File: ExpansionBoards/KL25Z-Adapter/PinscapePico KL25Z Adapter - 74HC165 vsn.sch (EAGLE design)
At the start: 26 parts, among them IC1 SN74HC165DR, IC2 SN74HC165DR, IC3 SN74HC165DR, IC4 LIS3DHTR, IC5 ADS1115IDGSR, IC6 PCA9555APW,118, SW1 TS-1187A-B-A-B

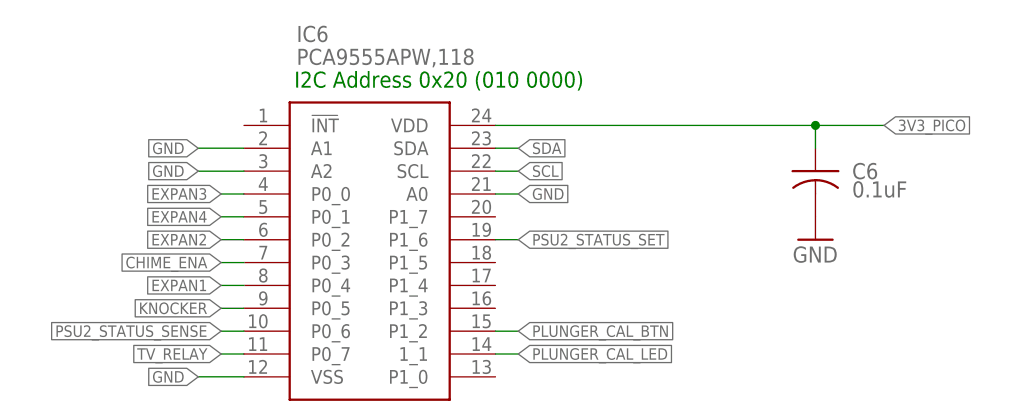
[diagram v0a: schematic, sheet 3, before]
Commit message: Finish JSON configuration for 74HC165, tweaks to 74HC165 layout
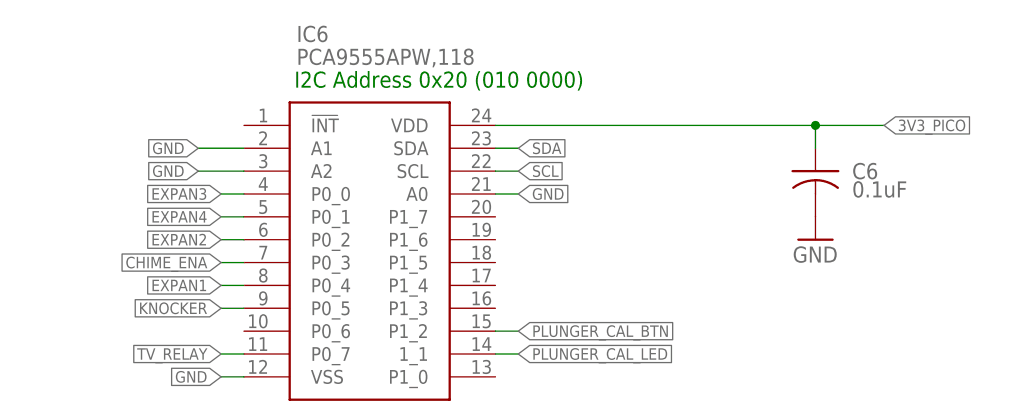
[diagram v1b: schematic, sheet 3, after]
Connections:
- net PSU2_STATUS_SENSE: now also RASPBERRY_PI_PICO.GP20; no longer IC6.P0_6
- net PSU2_STATUS_SET: now also RASPBERRY_PI_PICO.GP21; no longer IC6.P1_6
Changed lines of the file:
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@@
 <label x="246.38" y="101.6" size="1.27" layer="95" xref="yes"/>
+</segment>
+<segment>
+<pinref part="RASPBERRY_PI_PICO" gate="G$1" pin="GP21"/>
+<wire x1="73.66" y1="33.02" x2="71.12" y2="33.02" width="0.1524" layer="91"/>
+<label x="73.66" y="33.02" size="1.27" layer="95" xref="yes"/>
 </segment>
 </net>
@@
 <wire x1="243.84" y1="76.2" x2="246.38" y2="76.2" width="0.1524" layer="91"/>
 <label x="246.38" y="76.2" size="1.27" layer="95" xref="yes"/>
+</segment>
+<segment>
+<pinref part="RASPBERRY_PI_PICO" gate="G$1" pin="GP20"/>
+<wire x1="73.66" y1="30.48" x2="71.12" y2="30.48" width="0.1524" layer="91"/>
+<label x="73.66" y="30.48" size="1.27" layer="95" xref="yes"/>
 </segment>
 </net>
@@
 </segment>
 </net>
-<net name="PSU2_STATUS_SENSE" class="0">
-<segment>
-<pinref part="IC6" gate="G$1" pin="P0_6"/>
-<wire x1="30.48" y1="10.16" x2="27.94" y2="10.16" width="0.1524" layer="91"/>
-<label x="27.94" y="10.16" size="1.27" layer="95" rot="R180" xref="yes"/>
-</segment>
-</net>
-<net name="PSU2_STATUS_SET" class="0">
-<segment>
-<wire x1="58.42" y1="20.32" x2="60.96" y2="20.32" width="0.1524" layer="91"/>
-<label x="60.96" y="20.32" size="1.27" layer="95" xref="yes"/>
-<pinref part="IC6" gate="G$1" pin="P1_6"/>
-</segment>
-</net>
 <net name="CHIME_ENA" class="0">
 <segment>
@@
 <segment>
 <pinref part="IC6" gate="G$1" pin="VSS"/>
-<wire x1="25.4" y1="5.08" x2="30.48" y2="5.08" width="0.1524" layer="91"/>
-<label x="25.4" y="5.08" size="1.27" layer="95" rot="R180" xref="yes"/>
-</segment>
-<segment>
+<wire x1="27.94" y1="5.08" x2="30.48" y2="5.08" width="0.1524" layer="91"/>
+<label x="27.94" y="5.08" size="1.27" layer="95" rot="R180" xref="yes"/>
+</segment>
+<segment>

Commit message: minor board updates
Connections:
- net BUTTON12: now also IC2.F, RN2.4; no longer IC2.C, RN2.8
- net BUTTON13: now also IC2.C, RN2.8; no longer IC2.F, RN2.4
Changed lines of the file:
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@@
 <net name="BUTTON13" class="0">
+<segment>
+<wire x1="22.86" y1="43.18" x2="25.4" y2="43.18" width="0.1524" layer="91"/>
+<label x="22.86" y="43.18" size="1.27" layer="95" rot="R180" xref="yes"/>
+<pinref part="RN2" gate="G$1" pin="8"/>
+</segment>
+<segment>
+<wire x1="134.62" y1="50.8" x2="137.16" y2="50.8" width="0.1524" layer="91"/>
+<label x="137.16" y="50.8" size="1.27" layer="95" rot="MR180" xref="yes"/>
+<pinref part="IC2" gate="G$1" pin="C"/>
+</segment>
+</net>
+<net name="BUTTON12" class="0">
 <segment>
 <wire x1="53.34" y1="43.18" x2="50.8" y2="43.18" width="0.1524" layer="91"/>
@@
 </segment>
 </net>
-<net name="BUTTON12" class="0">
-<segment>
-<wire x1="22.86" y1="43.18" x2="25.4" y2="43.18" width="0.1524" layer="91"/>
-<label x="22.86" y="43.18" size="1.27" layer="95" rot="R180" xref="yes"/>
-<pinref part="RN2" gate="G$1" pin="8"/>
-</segment>
-<segment>
-<wire x1="134.62" y1="50.8" x2="137.16" y2="50.8" width="0.1524" layer="91"/>
-<label x="137.16" y="50.8" size="1.27" layer="95" rot="MR180" xref="yes"/>
-<pinref part="IC2" gate="G$1" pin="C"/>
-</segment>
-</net>

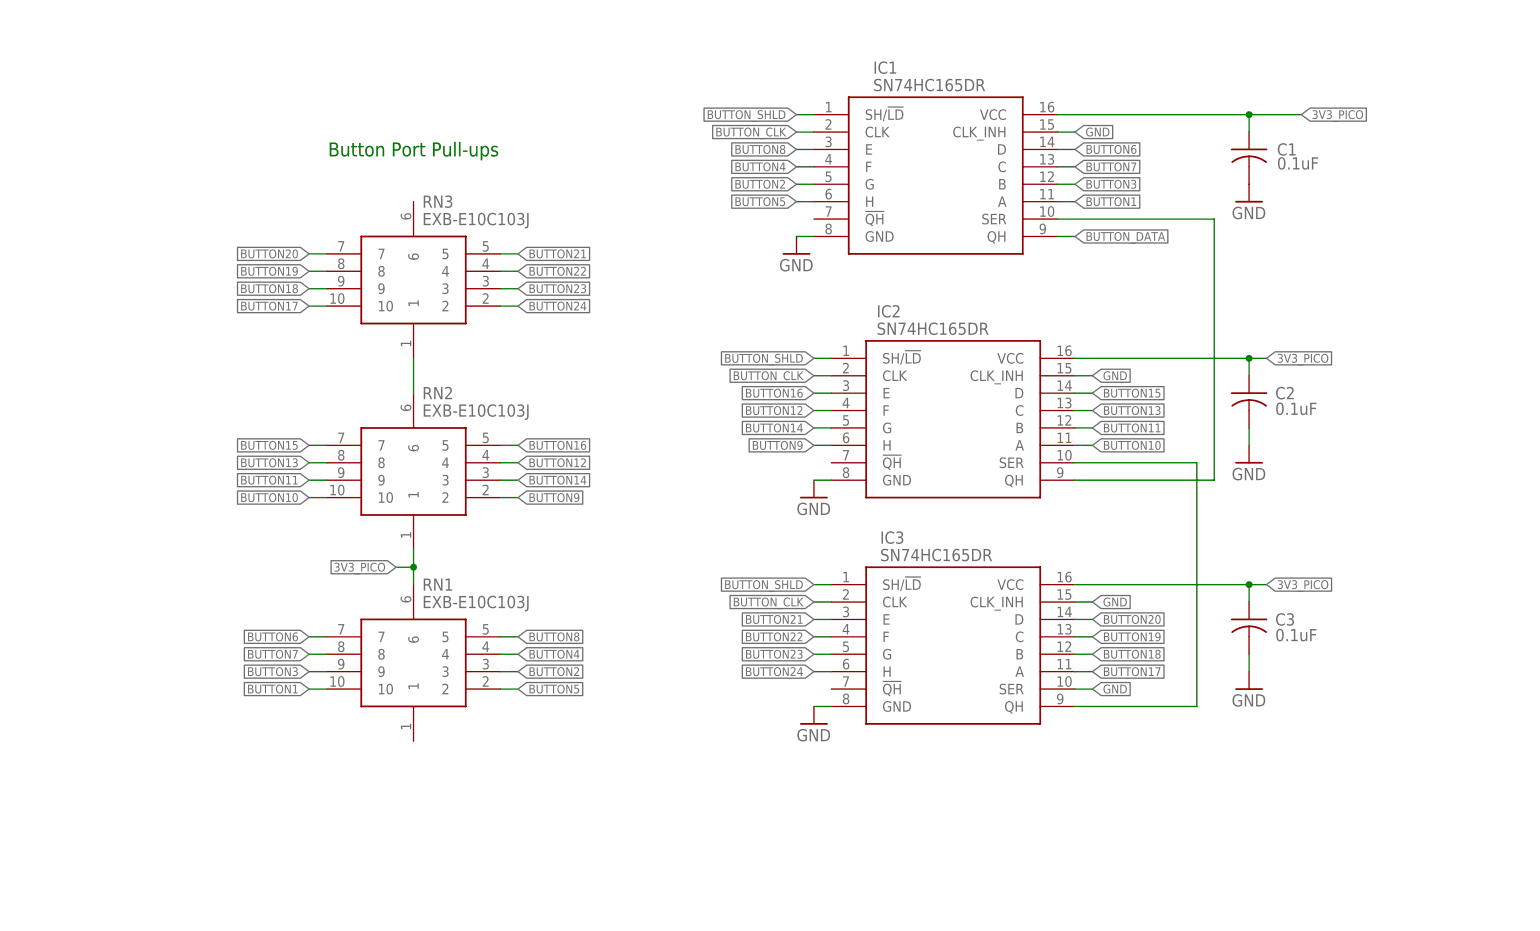
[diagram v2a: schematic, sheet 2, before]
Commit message: THT version of the board design
- Changed Pico footprint to THT
- Relocated components
- Relayouted traces.
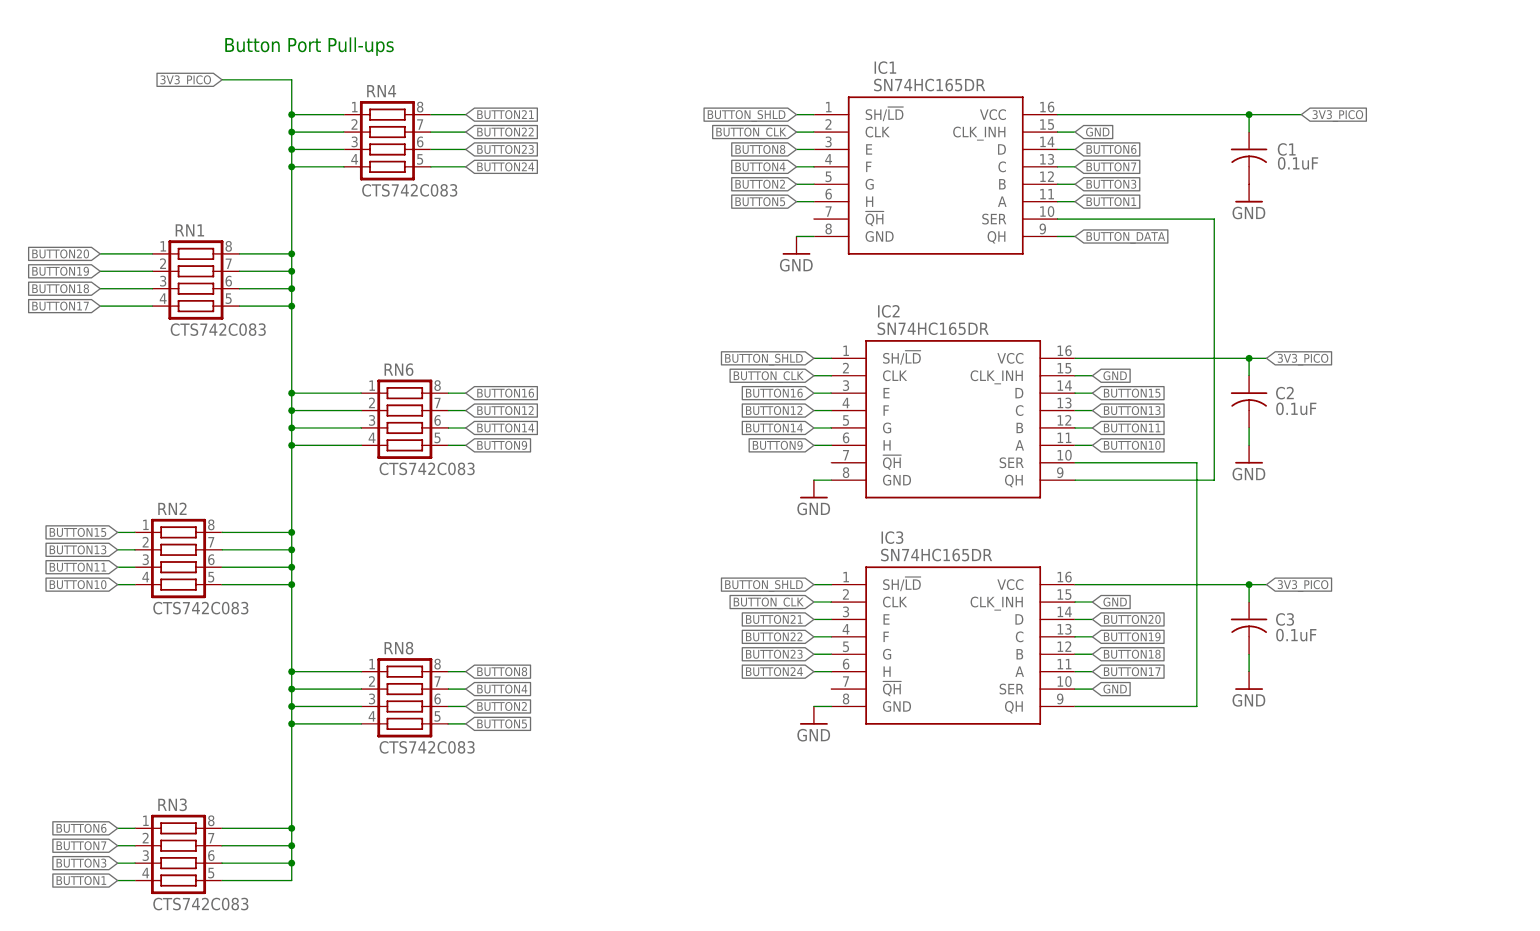
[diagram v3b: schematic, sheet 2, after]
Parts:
- added RN4, RN6, RN8: CTS742C083, resistor-net:CTS742C083
- RASPBERRY_PI_PICO: device RaspberryPi_Pico:RPI_PICO-SMD -> RaspberryPi_Pico:RPI_PICO-TH
- RN1, RN2, RN3: value EXB-E10C103J -> CTS742C083; device SamacSys_Parts:EXB-E10C103J -> resistor-net:CTS742C083
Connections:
- removed net N$2: RN2.6, RN3.1
- net 3V3_PICO: now also RN1.5, RN1.7, RN1.8, RN2.5, RN2.6, RN2.7, RN2.8, RN3.5, RN3.6, RN3.7, RN3.8, RN4.1, RN4.2, RN4.3, RN4.4, RN6.1, RN6.2, RN6.3, RN6.4, RN8.1, RN8.2, RN8.3, RN8.4; no longer RN2.1
- net BUTTON1: now also RN3.4; no longer RN1.10
- net BUTTON10: now also RN2.4; no longer RN2.10
- net BUTTON11: now also RN2.3; no longer RN2.9
- net BUTTON12: now also RN6.7; no longer RN2.4
- net BUTTON13: now also RN2.2; no longer RN2.8
- net BUTTON14: now also RN6.6; no longer RN2.3
- net BUTTON15: now also RN2.1; no longer RN2.7
- net BUTTON16: now also RN6.8; no longer RN2.5
- net BUTTON17: now also RN1.4; no longer RN3.10
- net BUTTON18: now also RN1.3; no longer RN3.9
- net BUTTON19: now also RN1.2; no longer RN3.8
- net BUTTON2: now also RN8.6; no longer RN1.3
- net BUTTON20: now also RN1.1; no longer RN3.7
- net BUTTON21: now also RN4.8; no longer RN3.5
- net BUTTON22: now also RN4.7; no longer RN3.4
- net BUTTON23: now also RN4.6; no longer RN3.3
- net BUTTON24: now also RN4.5; no longer RN3.2
- net BUTTON3: now also RN3.3; no longer RN1.9
- net BUTTON4: now also RN8.7; no longer RN1.4
- net BUTTON5: now also RN8.5; no longer RN1.2
- net BUTTON6: now also RN3.1; no longer RN1.7
- net BUTTON7: now also RN3.2; no longer RN1.8
- net BUTTON8: now also RN8.8; no longer RN1.5
- net BUTTON9: now also RN6.5; no longer RN2.2

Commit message: KL25Z adapter layout tweaks
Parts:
- RASPBERRY_PI_PICO: device RaspberryPi_Pico:RPI_PICO-TH -> RaspberryPi_Pico:RPI_PICO_NO_DEBUG
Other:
- note added: "Button Input Shift Registers"
- note added: "Install 0.1" pin headers on BOTTOM of board to mate with expansion board KL25Z sockets"
- note added: "Install 0.1" pin sockets on top of board to mate with 0.1" headers on bottom of Pico"
- note added: "KL25Z Compatible Connectors"
- note added: "NOTE: DO NOT INSTALL A KL25Z HERE! This whole board TAKES THE PLACE of a KL25Z. It DOESN'T connect to an actual KL25Z."
- note added: "RGB Status LED"
- note removed: "KL25Z Header Connectors Install 0.1" pin sockets on BOTTOM of board"
- moved on the sheet: C1, C2, C3, IC1, IC2, IC3, LED1, R1, R2, R3, R6, R7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

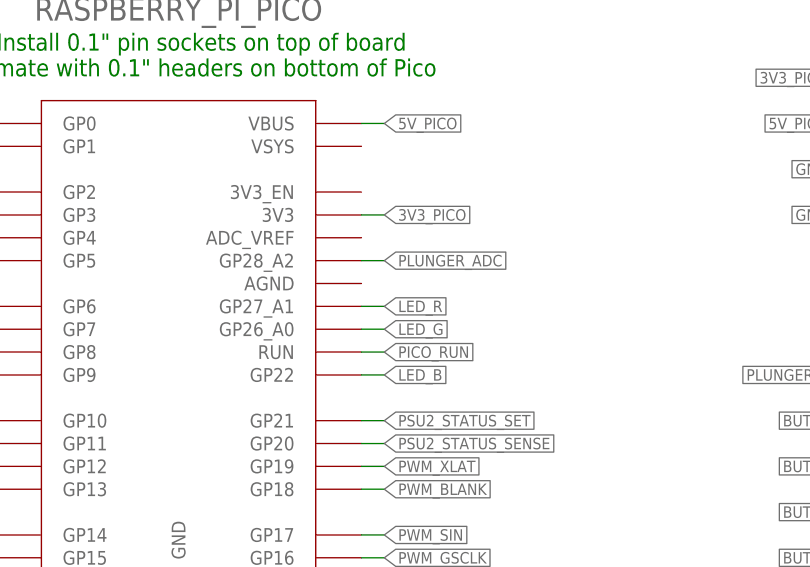
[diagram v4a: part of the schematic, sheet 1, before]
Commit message: KL25Z adapters - connect AGND to GND
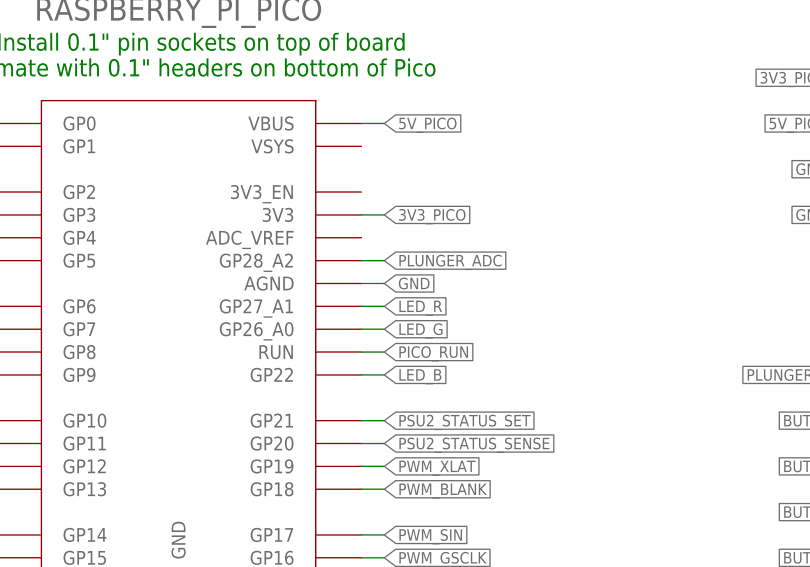
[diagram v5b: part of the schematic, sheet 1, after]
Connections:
- net GND: now also RASPBERRY_PI_PICO.AGND
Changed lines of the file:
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@@
 <label x="96.52" y="116.84" size="1.27" layer="95" rot="R270" xref="yes"/>
+</segment>
+<segment>
+<pinref part="RASPBERRY_PI_PICO" gate="G$1" pin="AGND"/>
+<wire x1="71.12" y1="48.26" x2="73.66" y2="48.26" width="0.1524" layer="91"/>
+<label x="73.66" y="48.26" size="1.27" layer="95" xref="yes"/>
 </segment>
 </net>
